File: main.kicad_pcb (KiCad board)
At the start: 2 copper layers, 120 x 100 mm, 21 parts, among them J1 Conn_01x01_Female, J2 Conn_01x01_Female, J3 Conn_01x01_Female, J4 Conn_01x01_Female, J5 Conn_01x01_Female, J6 Conn_01x01_Female, J7 Conn_Coaxial, Q1 AOT2618

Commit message: Added BOM
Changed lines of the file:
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@@
     (descr "CP, Radial series, Radial, pin pitch=5.00mm, , diameter=10mm, Electrolytic Capacitor")
     (tags "CP Radial series Radial pin pitch 5.00mm  diameter 10mm Electrolytic Capacitor")
-    (property "MFN" "Rubycon")
-    (property "PN" "160LEX33MEFC10X16")
+    (property "Alternative" "Rubycon 160LEX33MEFC10X16")
+    (property "MFN" "United Chemicon")
+    (property "PN" "EGXF351ELL330MJ35S")
     (property "Sheetfile" "main.kicad_sch")
     (property "Sheetname" "")
@@
     (descr "Capacitor SMD 1210 (3225 Metric), square (rectangular) end terminal, IPC_7351 nominal, (Body size source: IPC-SM-782 page 76, https://www.pcb-3d.com/wordpress/wp-content/uploads/ipc-sm-782a_amendment_1_and_2.pdf), generated with kicad-footprint-generator")
     (tags "capacitor")
+    (property "Alternative" "TDK CNC6P1X7R2A475K250AE")
     (property "MFN" "TDK")
-    (property "PN" "CNC6P1X7R2A475K250AE")
+    (property "PN" "CNA6P1X7R2A475K250AE")
     (property "Sheetfile" "main.kicad_sch")
     (property "Sheetname" "")
@@
     (descr "CP, Radial series, Radial, pin pitch=7.50mm, , diameter=18mm, Electrolytic Capacitor")
     (tags "CP Radial series Radial pin pitch 7.50mm  diameter 18mm Electrolytic Capacitor")
+    (property "Alternative" "United Chemicon EKYB101ELL102MM40S")
     (property "MFN" "Nichicon")
     (property "PN" "UPW2A102MHD")
@@
     (property "Sheetfile" "main.kicad_sch")
     (property "Sheetname" "")
-    (attr exclude_from_pos_files)
+    (property "exclude_from_bom" "")
+    (attr exclude_from_pos_files exclude_from_bom)
     (fp_text reference "LOGO2" (at 0 0) (layer "F.SilkS") hide
       (effects (font (size 1 1) (thickness 0.15)))
@@
     (descr "Resistor SMD 0805 (2012 Metric), square (rectangular) end terminal, IPC_7351 nominal, (Body size source: IPC-SM-782 page 72, https://www.pcb-3d.com/wordpress/wp-content/uploads/ipc-sm-782a_amendment_1_and_2.pdf), generated with kicad-footprint-generator")
     (tags "resistor")
+    (property "Alternative" "Panasonic ERJ-6ENF1002V")
+    (property "MFN" "Yageo")
+    (property "PN" "AC0805FR-0710KL")
     (property "Sheetfile" "main.kicad_sch")
     (property "Sheetname" "")
@@
     (descr "Capacitor SMD 1206 (3216 Metric), square (rectangular) end terminal, IPC_7351 nominal, (Body size source: IPC-SM-782 page 76, https://www.pcb-3d.com/wordpress/wp-content/uploads/ipc-sm-782a_amendment_1_and_2.pdf), generated with kicad-footprint-generator")
     (tags "capacitor")
+    (property "Alternative" "TDK CGA5L2X7R2A105K160AA")
     (property "MFN" "TDK")
     (property "PN" "CGA5L2X7R2A105M160AE")
@@
     (descr "Capacitor SMD 1206 (3216 Metric), square (rectangular) end terminal, IPC_7351 nominal, (Body size source: IPC-SM-782 page 76, https://www.pcb-3d.com/wordpress/wp-content/uploads/ipc-sm-782a_amendment_1_and_2.pdf), generated with kicad-footprint-generator")
     (tags "capacitor")
+    (property "Alternative" "TDK CGA5L2X7R2A105K160AA")
     (property "MFN" "TDK")
     (property "PN" "CGA5L2X7R2A105M160AE")
@@
     (property "Sheetfile" "main.kicad_sch")
     (property "Sheetname" "")
-    (attr exclude_from_pos_files)
+    (property "exclude_from_bom" "")
+    (attr exclude_from_pos_files exclude_from_bom)
     (fp_text reference "LOGO1" (at 0 0) (layer "F.SilkS") hide
       (effects (font (size 1 1) (thickness 0.15)))
@@
     (fp_arc (start 21.465279 -4.307629) (mid 21.535978 -3.545533) (end 21.047085 -2.956661) (layer "F.SilkS") (width 0.12))
     (fp_arc (start -21.067316 4.100505) (mid -21.145601 3.365146) (end -20.696747 2.777429) (layer "F.SilkS") (width 0.12))
-    (fp_arc (start 19.058317 -9.075185) (mid 19.74445 -9.414242) (end 20.469421 -9.168911) (layer "F.SilkS") (width 0.12))
+    (fp_arc (start 19.058317 -9.075185) (mid 19.74446 -9.41424) (end 20.469421 -9.168911) (layer "F.SilkS") (width 0.12))
     (fp_arc (start 16.386175 -12.20573) (mid 16.926425 -12.747869) (end 17.691791 -12.749206) (layer "F.SilkS") (width 0.12))
     (fp_arc (start -8.1 -7) (mid -8.187868 -6.787868) (end -8.4 -6.7) (layer "F.SilkS") (width 0.12))
@@
     (fp_arc (start 10.5 -13) (mid 11.207107 -12.707107) (end 11.5 -12) (layer "F.SilkS") (width 0.12))
     (fp_arc (start 14.8 11.9) (mid 14.507107 12.607107) (end 13.8 12.9) (layer "F.SilkS") (width 0.12))
-    (fp_arc (start -17.691791 -12.749206) (mid -16.926426 -12.74787) (end -16.386175 -12.20573) (layer "F.SilkS") (width 0.12))
+    (fp_arc (start -17.691791 -12.749206) (mid -16.926425 -12.74787) (end -16.386175 -12.20573) (layer "F.SilkS") (width 0.12))
     (fp_arc (start 20.774322 9.592377) (mid 20.052858 9.847847) (end 19.362046 9.518363) (layer "F.SilkS") (width 0.12))
     (fp_arc (start -21.047085 -2.956661) (mid -21.535977 -3.545534) (end -21.465279 -4.307629) (layer "F.SilkS") (width 0.12))
@@
     (fp_arc (start 8.4 -6.2) (mid 7.834315 -6.434315) (end 7.6 -7) (layer "F.Fab") (width 0.1))
     (fp_arc (start -11 -11.8) (mid -10.803962 -12.285821) (end -10.325651 -12.49953) (layer "F.Fab") (width 0.1))
-    (fp_arc (start 12.79953 -11.8) (mid 13.004551 -12.294999) (end 13.49953 -12.5) (layer "F.Fab") (width 0.1))
+    (fp_arc (start 12.79953 -11.8) (mid 13.004541 -12.294989) (end 13.49953 -12.5) (layer "F.Fab") (width 0.1))
     (fp_arc (start 12.8 -7) (mid 12.565685 -6.434315) (end 12 -6.2) (layer "F.Fab") (width 0.1))
     (fp_arc (start 13.374349 12.49953) (mid 12.896038 12.285821) (end 12.7 11.8) (layer "F.Fab") (width 0.1))
     (fp_arc (start 11.8 -6.2) (mid 11.234315 -6.434315) (end 11 -7) (layer "F.Fab") (width 0.1))
     (fp_arc (start -12 -6.2) (mid -12.565685 -6.434315) (end -12.8 -7) (layer "F.Fab") (width 0.1))
-    (fp_arc (start 13.725181 -12.49953) (mid 14.203509 -12.285818) (end 14.39953 -11.8) (layer "F.Fab") (width 0.1))
+    (fp_arc (start 13.725181 -12.49953) (mid 14.203536 -12.285845) (end 14.39953 -11.8) (layer "F.Fab") (width 0.1))
     (fp_arc (start -13.49953 -12.5) (mid -13.004555 -12.294975) (end -12.79953 -11.8) (layer "F.Fab") (width 0.1))
     (fp_arc (start -14.39953 -11.8) (mid -14.203492 -12.285821) (end -13.725181 -12.49953) (layer "F.Fab") (width 0.1))
     (fp_arc (start -13.60047 12.5) (mid -14.095445 12.294975) (end -14.30047 11.8) (layer "F.Fab") (width 0.1))
-    (fp_arc (start 14.30047 11.8) (mid 14.095449 12.294999) (end 13.60047 12.5) (layer "F.Fab") (width 0.1))
+    (fp_arc (start 14.30047 11.8) (mid 14.095459 12.294989) (end 13.60047 12.5) (layer "F.Fab") (width 0.1))
     (fp_arc (start -7.6 -7) (mid -7.834315 -6.434315) (end -8.4 -6.2) (layer "F.Fab") (width 0.1))
     (fp_arc (start 6.925651 -12.49953) (mid 7.403962 -12.285821) (end 7.6 -11.8) (layer "F.Fab") (width 0.1))
@@
     (descr "Resistor SMD 1206 (3216 Metric), square (rectangular) end terminal, IPC_7351 nominal, (Body size source: IPC-SM-782 page 72, https://www.pcb-3d.com/wordpress/wp-content/uploads/ipc-sm-782a_amendment_1_and_2.pdf), generated with kicad-footprint-generator")
     (tags "resistor")
-    (property "MFN" "Susumu")
-    (property "PN" "RG3216P-49R9-B-T5")
+    (property "Alternative" "Panasonic ERJ-U08F49R9V")
+    (property "MFN" "Yageo")
+    (property "PN" "AC1206FR-0749R9L")
     (property "Sheetfile" "main.kicad_sch")
     (property "Sheetname" "")
@@
     (descr "Resistor SMD 1206 (3216 Metric), square (rectangular) end terminal, IPC_7351 nominal, (Body size source: IPC-SM-782 page 72, https://www.pcb-3d.com/wordpress/wp-content/uploads/ipc-sm-782a_amendment_1_and_2.pdf), generated with kicad-footprint-generator")
     (tags "resistor")
-    (property "MFN" "Susumu")
-    (property "PN" "RG3216P-49R9-B-T5")
+    (property "Alternative" "Panasonic ERJ-U08F49R9V")
+    (property "MFN" "Yageo")
+    (property "PN" "AC1206FR-0749R9L")
     (property "Sheetfile" "main.kicad_sch")
     (property "Sheetname" "")
@@
     (descr "Resistor SMD 1206 (3216 Metric), square (rectangular) end terminal, IPC_7351 nominal, (Body size source: IPC-SM-782 page 72, https://www.pcb-3d.com/wordpress/wp-content/uploads/ipc-sm-782a_amendment_1_and_2.pdf), generated with kicad-footprint-generator")
     (tags "resistor")
-    (property "MFN" "Susumu")
-    (property "PN" "RG3216P-49R9-B-T5")
+    (property "Alternative" "Panasonic ERJ-U08F49R9V")
+    (property "MFN" "Yageo")
+    (property "PN" "AC1206FR-0749R9L")
     (property "Sheetfile" "main.kicad_sch")
     (property "Sheetname" "")

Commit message: Updated footprints
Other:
- board text added: "Remember: Add thermal compound or a thermal pad between the MOSFET and the heatsink"
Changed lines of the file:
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@@
     (property "Sheetname" "")
     (attr through_hole)
-    (fp_text reference "HS1" (at -0.025 -3.5) (layer "F.SilkS")
+    (fp_text reference "HS1" (at -0.025 -4) (layer "F.SilkS")
       (effects (font (size 1 1) (thickness 0.15)))
     )
@@
     (fp_arc (start 21.465279 -4.307629) (mid 21.535978 -3.545533) (end 21.047085 -2.956661) (layer "F.SilkS") (width 0.12))
     (fp_arc (start -21.067316 4.100505) (mid -21.145601 3.365146) (end -20.696747 2.777429) (layer "F.SilkS") (width 0.12))
-    (fp_arc (start 19.058317 -9.075185) (mid 19.74446 -9.41424) (end 20.469421 -9.168911) (layer "F.SilkS") (width 0.12))
+    (fp_arc (start 19.058317 -9.075185) (mid 19.74446 -9.414236) (end 20.469421 -9.168911) (layer "F.SilkS") (width 0.12))
     (fp_arc (start 16.386175 -12.20573) (mid 16.926425 -12.747869) (end 17.691791 -12.749206) (layer "F.SilkS") (width 0.12))
     (fp_arc (start -8.1 -7) (mid -8.187868 -6.787868) (end -8.4 -6.7) (layer "F.SilkS") (width 0.12))
@@
     (fp_arc (start 10.5 -13) (mid 11.207107 -12.707107) (end 11.5 -12) (layer "F.SilkS") (width 0.12))
     (fp_arc (start 14.8 11.9) (mid 14.507107 12.607107) (end 13.8 12.9) (layer "F.SilkS") (width 0.12))
-    (fp_arc (start -17.691791 -12.749206) (mid -16.926425 -12.74787) (end -16.386175 -12.20573) (layer "F.SilkS") (width 0.12))
+    (fp_arc (start -17.691791 -12.749206) (mid -16.926426 -12.74787) (end -16.386175 -12.20573) (layer "F.SilkS") (width 0.12))
     (fp_arc (start 20.774322 9.592377) (mid 20.052858 9.847847) (end 19.362046 9.518363) (layer "F.SilkS") (width 0.12))
     (fp_arc (start -21.047085 -2.956661) (mid -21.535977 -3.545534) (end -21.465279 -4.307629) (layer "F.SilkS") (width 0.12))
@@
     (fp_arc (start 11.8 -6.2) (mid 11.234315 -6.434315) (end 11 -7) (layer "F.Fab") (width 0.1))
     (fp_arc (start -12 -6.2) (mid -12.565685 -6.434315) (end -12.8 -7) (layer "F.Fab") (width 0.1))
-    (fp_arc (start 13.725181 -12.49953) (mid 14.203536 -12.285845) (end 14.39953 -11.8) (layer "F.Fab") (width 0.1))
+    (fp_arc (start 13.725181 -12.49953) (mid 14.203563 -12.285871) (end 14.39953 -11.8) (layer "F.Fab") (width 0.1))
     (fp_arc (start -13.49953 -12.5) (mid -13.004555 -12.294975) (end -12.79953 -11.8) (layer "F.Fab") (width 0.1))
     (fp_arc (start -14.39953 -11.8) (mid -14.203492 -12.285821) (end -13.725181 -12.49953) (layer "F.Fab") (width 0.1))
@@
     (effects (font (size 1 1) (thickness 0.15)) (justify left))
   )
+  (gr_text "Remember: Add thermal compound or a thermal\npad between the MOSFET and the heatsink" (at 81.06 146.355) (layer "F.Fab")
+    (effects (font (size 2 2) (thickness 0.3)) (justify left))
+  )
   (gr_text "35 µm" (at 246.06 91.355) (layer "F.Fab")

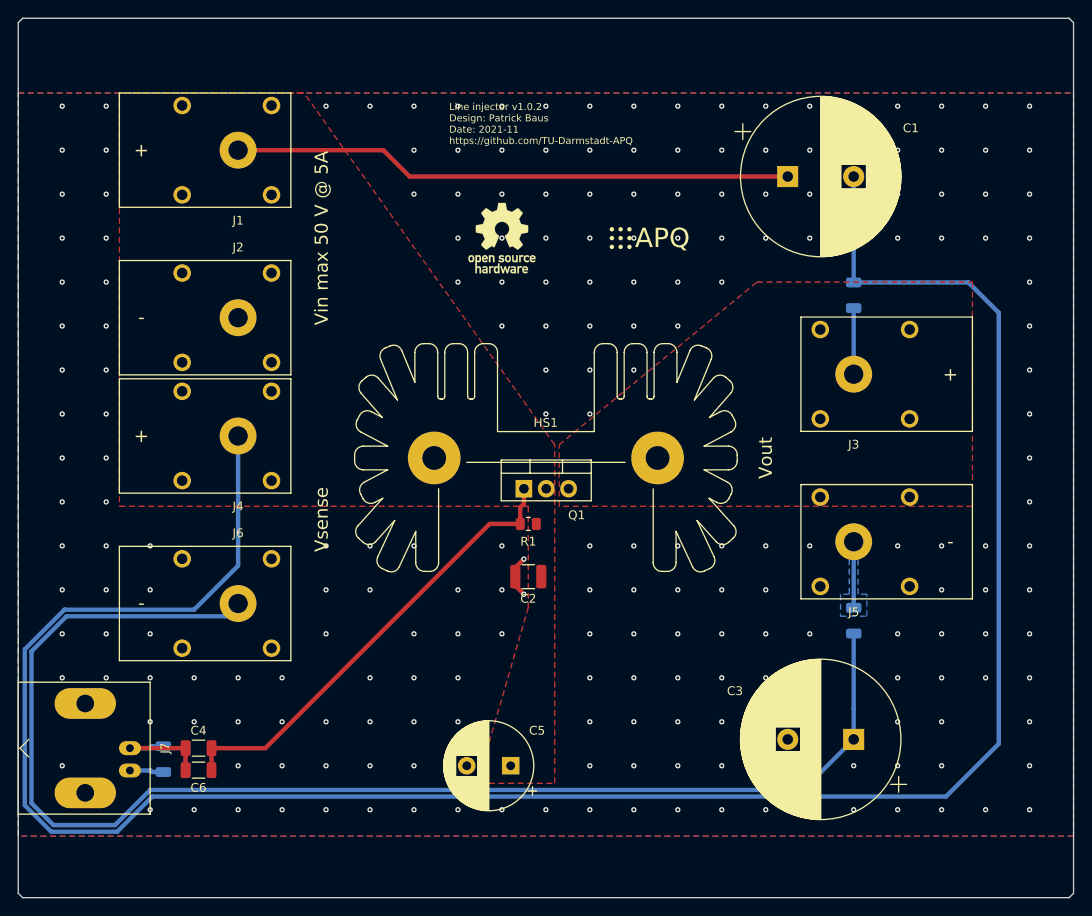
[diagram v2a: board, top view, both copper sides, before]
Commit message: Update to KiCad 8
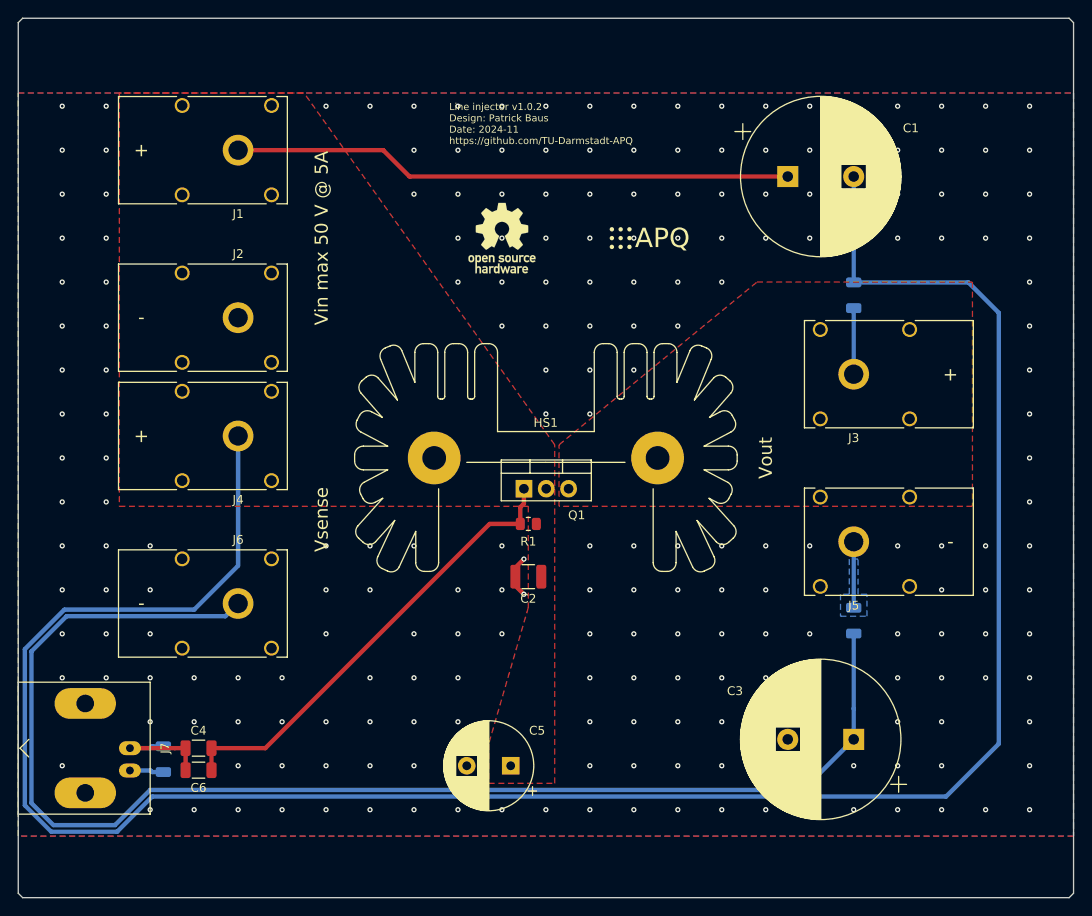
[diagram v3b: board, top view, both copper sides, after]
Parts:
- J1, J3, J4: footprint Custom_footprints:Schuetzinger_4mm_Jack -> Connector:Banana_Cliff_FCR7350R_S16N-PC_Horizontal
- J2, J5, J6: footprint Custom_footprints:Schuetzinger_4mm_Jack -> Connector:Banana_Cliff_FCR7350B_S16N-PC_Horizontal
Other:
- board text added: "Line injector v1.0.2 Design: Patrick Baus Date: 2024-11 https://github.com/TU-Darmstadt-APQ"
- board text removed: "Line injector v1.0.2 Design: Patrick Baus Date: 2021-11 https://github.com/TU-Darmstadt-APQ"

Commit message: Updated libs (#2)
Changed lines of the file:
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@@
 	(net 7 "unconnected-(HS1-Pad1)")
 	(net 8 "Net-(J3-Pin_1)")
+	(net 9 "unconnected-(HS1-Pad1)_1")
 	(footprint "Capacitor_THT:CP_Radial_D10.0mm_P5.00mm"
 		(layer "F.Cu")
@@
 			)
 		)
-		(property "Description" ""
+		(property "Description" "Generic connector, single row, 01x01, script generated"
 			(at 0 0 0)
 			(unlocked yes)
@@
 			)
 		)
-		(property ki_fp_filters "Connector*:*")
+		(property ki_fp_filters "Connector*:*_1x??_*")
 		(sheetname "Root")
 		(sheetfile "main.kicad_sch")
@@
 			)
 		)
-		(property "Description" ""
+		(property "Description" "Generic connector, single row, 01x01, script generated"
 			(at 0 0 0)
 			(unlocked yes)
@@
 			)
 		)
-		(property ki_fp_filters "Connector*:*")
+		(property ki_fp_filters "Connector*:*_1x??_*")
 		(sheetname "Root")
 		(sheetfile "main.kicad_sch")
@@
 			)
 		)
-		(property "Description" ""
+		(property "Description" "Open Hardware logo, small"
 			(at 0 0 0)
 			(layer "F.Fab")
@@
 			)
 		)
-		(property "exclude_from_bom" ""
-			(at 0 0 0)
-			(layer "F.Fab")
-			(hide yes)
-			(effects
-				(font
-					(size 1 1)
-					(thickness 0.15)
-				)
-			)
-		)
 		(sheetname "Root")
 		(sheetfile "main.kicad_sch")
@@
 			)
 		)
-		(property "Description" ""
+		(property "Description" "Generic connector, single row, 01x01, script generated"
 			(at 0 0 0)
 			(unlocked yes)
@@
 			)
 		)
-		(property ki_fp_filters "Connector*:*")
+		(property ki_fp_filters "Connector*:*_1x??_*")
 		(sheetname "Root")
 		(sheetfile "main.kicad_sch")
@@
 			)
 		)
-		(property "Datasheet" " ~"
+		(property "Datasheet" ""
 			(at 0 0 90)
 			(layer "F.Fab")
@@
 			)
 		)
-		(property "Description" ""
+		(property "Description" "coaxial connector (BNC, SMA, SMB, SMC, Cinch/RCA, LEMO, ...)"
 			(at 0 0 90)
 			(layer "F.Fab")
@@
 			)
 		)
-		(property ki_fp_filters "*BNC* *SMA* *SMB* *SMC* *Cinch* *LEMO*")
+		(property ki_fp_filters "*BNC* *SMA* *SMB* *SMC* *Cinch* *LEMO* *UMRF* *MCX* *U.FL*")
 		(sheetname "Root")
 		(sheetfile "main.kicad_sch")
@@
 			)
 		)
+		(model "${KIPRJMOD}/footprints_project_specific.3dshapes/bnc_90_1-1337543-0.wrl"
+			(offset
+				(xyz 0 12.54 0)
+			)
+			(scale
+				(xyz 1 1 1)
+			)
+			(rotate
+				(xyz 0 0 180)
+			)
+		)
 	)
 	(footprint "Connector:Banana_Cliff_FCR7350B_S16N-PC_Horizontal"
@@
 			)
 		)
-		(property "Description" ""
+		(property "Description" "Generic connector, single row, 01x01, script generated"
 			(at 0 0 180)
 			(unlocked yes)
@@
 			)
 		)
-		(property ki_fp_filters "Connector*:*")
+		(property ki_fp_filters "Connector*:*_1x??_*")
 		(sheetname "Root")
 		(sheetfile "main.kicad_sch")
@@
 			)
 		)
-		(property "Description" ""
+		(property "Description" "Generic connector, single row, 01x01, script generated"
 			(at 0 0 180)
 			(unlocked yes)
@@
 			)
 		)
-		(property ki_fp_filters "Connector*:*")
+		(property ki_fp_filters "Connector*:*_1x??_*")
 		(sheetname "Root")
 		(sheetfile "main.kicad_sch")
@@
 		(fp_arc
 			(start -17.691791 -12.749206)
-			(mid -16.926425 -12.74787)
+			(mid -16.926426 -12.74787)
 			(end -16.386175 -12.20573)
 			(stroke
@@
 		(fp_arc
 			(start 18.007467 12.859044)
-			(mid 17.24283 12.892429)
+			(mid 17.242829 12.892428)
 			(end 16.678541 12.375356)
 			(stroke
@@
 		(fp_arc
 			(start 19.058317 -9.075185)
-			(mid 19.74445 -9.414276)
+			(mid 19.74445 -9.414242)
 			(end 20.469421 -9.168911)
 			(stroke
@@
 		(fp_arc
 			(start 19.834479 -5.256572)
-			(mid 20.59659 -5.327292)
+			(mid 20.596584 -5.327302)
 			(end 21.185447 -4.838378)
 			(stroke
@@
 		(fp_arc
 			(start 9.39953 -11.8)
-			(mid 9.604557 -12.294964)
+			(mid 9.604561 -12.294969)
 			(end 10.09953 -12.5)
 			(stroke
@@
 		(fp_arc
 			(start 12.79953 -11.8)
-			(mid 13.004557 -12.294964)
+			(mid 13.004551 -12.294999)
 			(end 13.49953 -12.5)
 			(stroke
@@
 		(fp_arc
 			(start 13.725181 -12.49953)
-			(mid 14.203473 -12.285811)
+			(mid 14.203509 -12.285818)
 			(end 14.39953 -11.8)
 			(stroke
@@
 		(fp_arc
 			(start 14.30047 11.8)
-			(mid 14.095443 12.294964)
+			(mid 14.095449 12.294999)
 			(end 13.60047 12.5)
 			(stroke
@@
 			(layers "*.Cu" "*.Mask")
 			(remove_unused_layers no)
-			(net 7 "unconnected-(HS1-Pad1)")
+			(net 9 "unconnected-(HS1-Pad1)_1")
 			(pintype "passive+no_connect")
 		)
@@
 			)
 		)
-		(property "Description" ""
+		(property "Description" "Generic connector, single row, 01x01, script generated"
 			(at 0 0 0)
 			(unlocked yes)
@@
 			)
 		)
-		(property ki_fp_filters "Connector*:*")
+		(property ki_fp_filters "Connector*:*_1x??_*")
 		(sheetname "Root")
 		(sheetfile "main.kicad_sch")
